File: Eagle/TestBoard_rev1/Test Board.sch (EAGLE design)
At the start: 9 parts

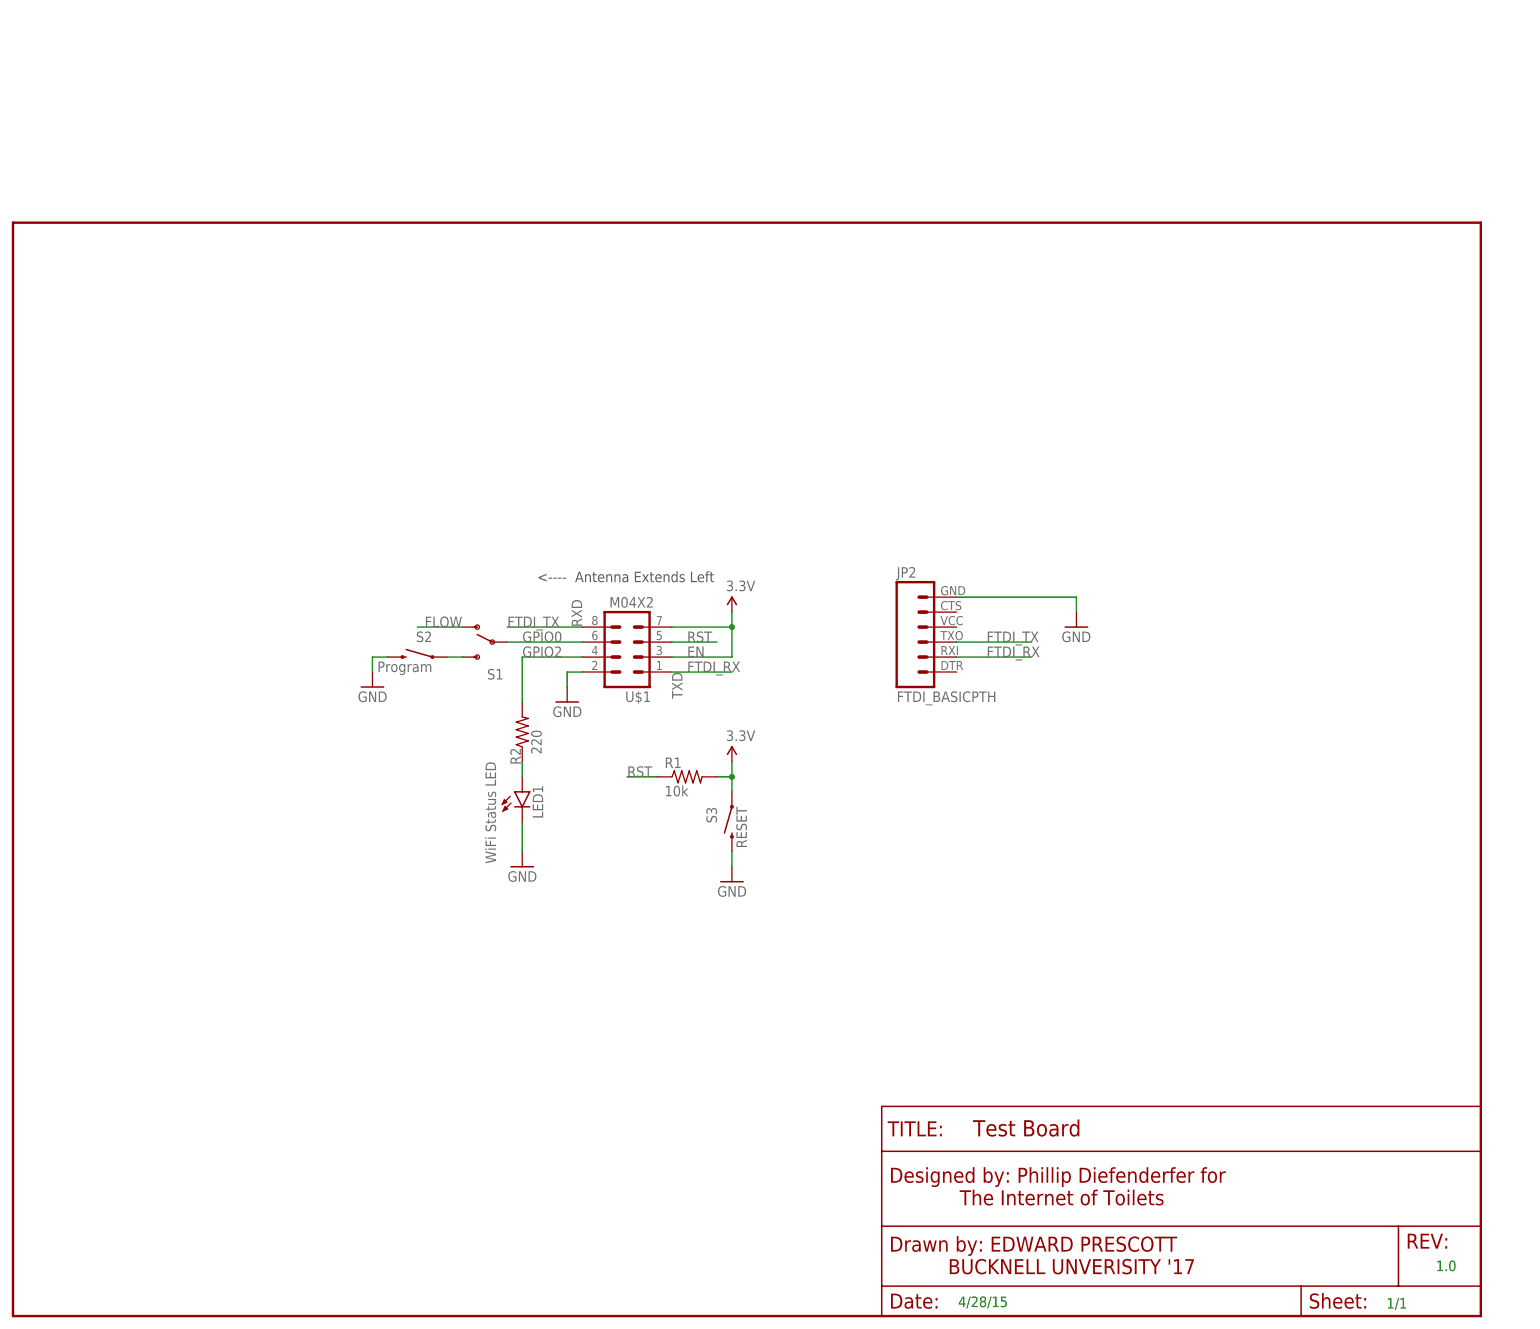
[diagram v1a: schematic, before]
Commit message: Rev 0.1 Carrier Board ready for Proto-Run
The Rev 0.1 Carrier board is just about ready for a prototype run on the
PCB mill and is designed for a mill with no silk or solder mask. Changes
include an edited schematic to include a better ESP part. power
considerations, and some formatting for readability. A first-run
mill-able board has been prepared as well. Finally, the Git Ignore was
modified to ignore temporary Eagle Files.
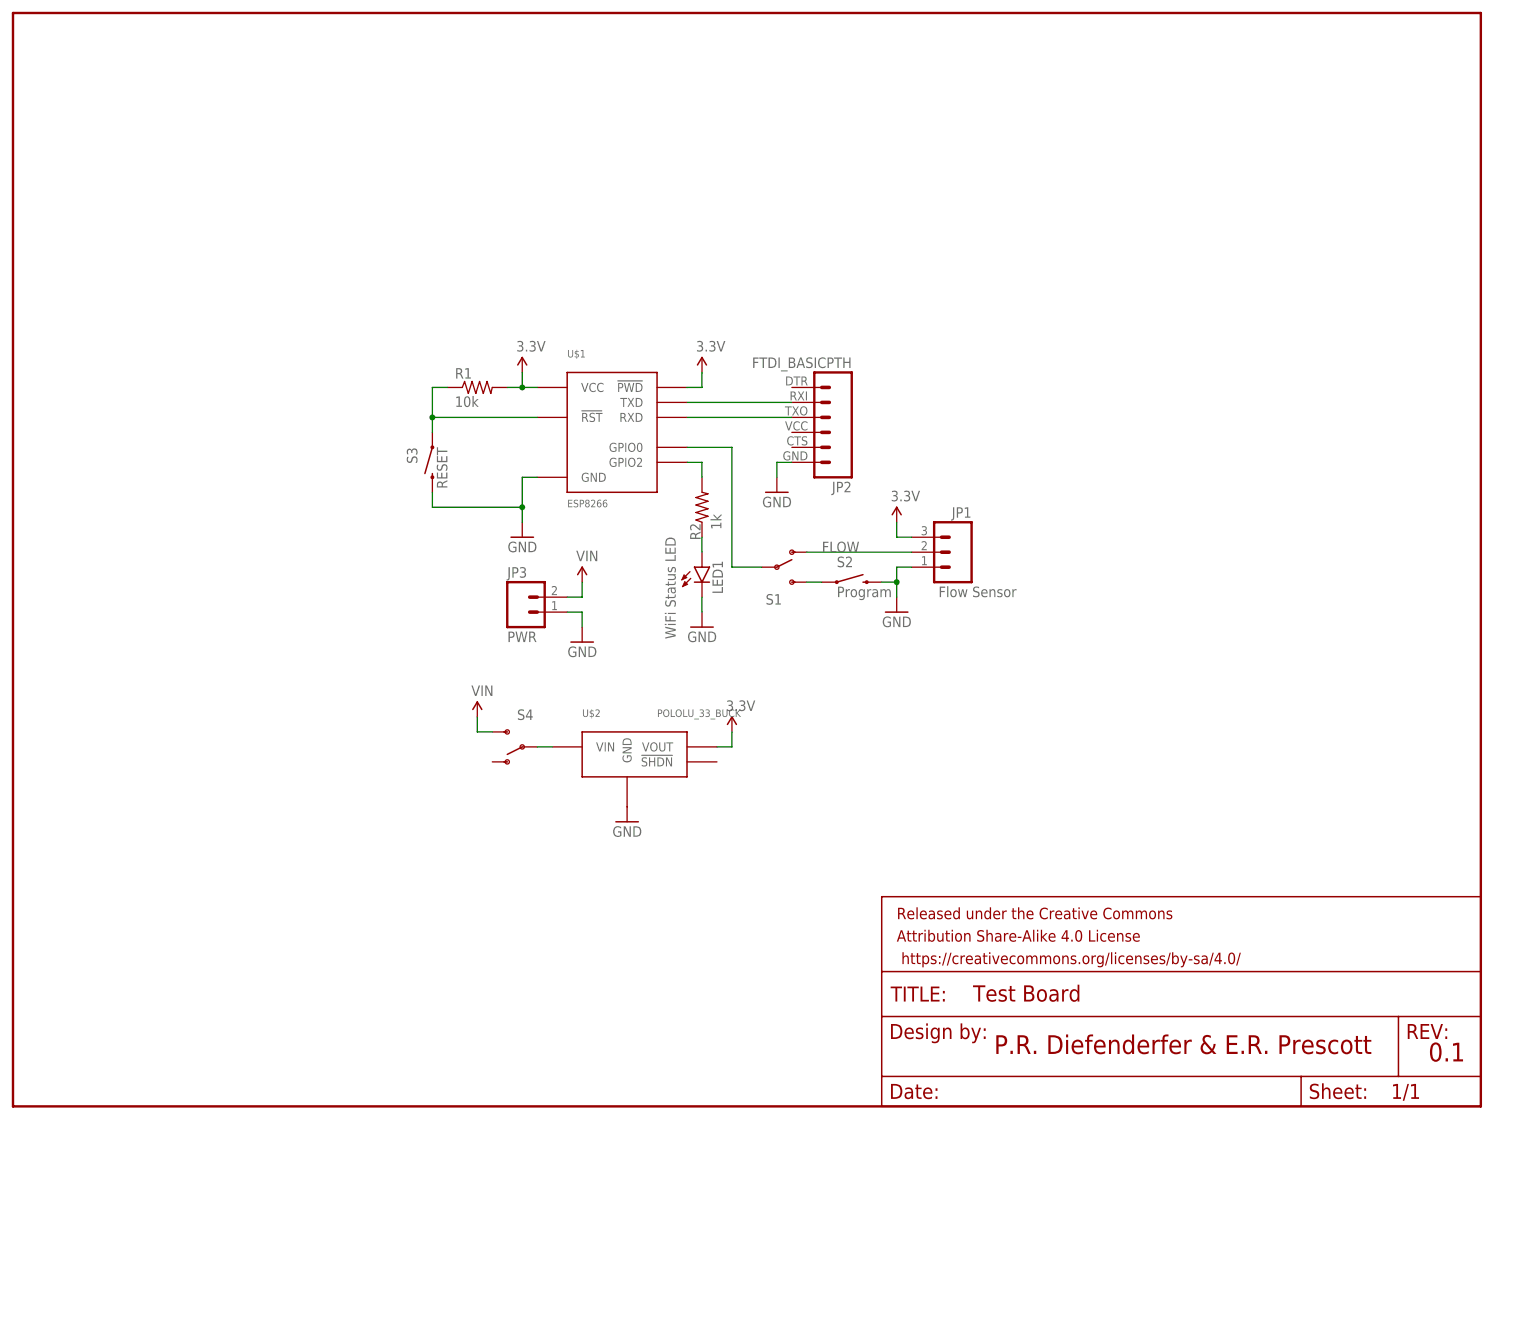
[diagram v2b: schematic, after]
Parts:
- added JP1: Flow Sensor, SparkFun-Connectors:M03LOCK
- added JP3: PWR, SparkFun-Connectors:M02LOCK
- added S4: (no value), SparkFun-Electromechanical:SWITCH-SPDTPTH
- added U$2: POLOLU_33_BUCK, dCustom:POLOLU_33_BUCK
- R2: value 220 -> 1k
- U$1: value M04X2 -> ESP8266; device SparkFun-Connectors:M04X2 -> dCustom:ESP8266_R3
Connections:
- removed net FTDI_RX: JP2.2, U$1.1
- removed net FTDI_TX: JP2.3, U$1.8
- removed net GPIO0: S1.P, U$1.6
- removed net GPIO2: R2.2, U$1.4
- removed net RST: R1.1, U$1.5
- new net N$2: JP2.2, U$1.TXD
- new net N$3: R1.1, S3.1, U$1.!RST
- new net N$4: JP2.3, U$1.RXD
- new net N$6: R2.2, U$1.GPIO2
- new net N$7: S1.P, U$1.GPIO0
- new net N$8: S4.P, U$2.VIN
- new net VIN: JP3.2, S4.S
- net 3.3V: now also JP1.3, U$1.!PWD, U$1.VCC, U$2.VOUT; no longer S3.1, U$1.3, U$1.7
- net FLOW: now also JP1.2
- net GND: now also JP1.1, JP3.1, U$1.GND, U$2.GND; no longer U$1.2
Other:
- note added: "0.1"
- note added: "P.R. Diefenderfer & E.R. Prescott"
- note removed: "1.0"
- note removed: "1/1"
- note removed: "4/28/15"
- note removed: "<---- Antenna Extends Left"
- note removed: "EN"
- note removed: "RXD"
- note removed: "TXD"
- moved on the sheet: JP2, LED1, R1, R2, S1, S2, S3
